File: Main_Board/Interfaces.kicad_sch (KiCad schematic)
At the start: 17 parts, among them J4 External bords interfaces, Q2 2N7002

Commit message: Fix schematic readibility
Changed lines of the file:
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@@
 	(wire
 		(pts
-			(xy 26.67 44.45) (xy 26.67 82.55)
+			(xy 30.48 44.45) (xy 30.48 82.55)
 		)
 		(stroke
@@
 	(wire
 		(pts
-			(xy 123.19 140.97) (xy 127 140.97)
+			(xy 91.44 137.16) (xy 95.25 137.16)
 		)
 		(stroke
@@
 	(wire
 		(pts
-			(xy 123.19 132.08) (xy 127 132.08)
+			(xy 91.44 128.27) (xy 95.25 128.27)
 		)
 		(stroke
@@
 	(wire
 		(pts
-			(xy 77.47 142.24) (xy 85.09 142.24)
+			(xy 45.72 138.43) (xy 53.34 138.43)
 		)
 		(stroke
@@
 	(wire
 		(pts
-			(xy 31.75 44.45) (xy 31.75 80.01)
+			(xy 35.56 44.45) (xy 35.56 80.01)
 		)
 		(stroke
@@
 	(wire
 		(pts
-			(xy 31.75 80.01) (xy 121.92 80.01)
+			(xy 35.56 80.01) (xy 121.92 80.01)
 		)
 		(stroke
@@
 	(wire
 		(pts
-			(xy 77.47 132.08) (xy 85.09 132.08)
+			(xy 45.72 128.27) (xy 53.34 128.27)
 		)
 		(stroke
@@
 	(wire
 		(pts
-			(xy 77.47 137.16) (xy 85.09 137.16)
+			(xy 45.72 133.35) (xy 53.34 133.35)
 		)
 		(stroke
@@
 	(wire
 		(pts
-			(xy 26.67 82.55) (xy 142.24 82.55)
+			(xy 30.48 82.55) (xy 142.24 82.55)
 		)
 		(stroke
@@
 	)
 	(label "B_RS485"
-		(at 127 140.97 0)
+		(at 95.25 137.16 0)
 		(effects
 			(font
@@
 	)
 	(label "A_RS485"
-		(at 127 132.08 0)
+		(at 95.25 128.27 0)
 		(effects
 			(font
@@
 	(hierarchical_label "MODULE_BUS_RX"
 		(shape input)
-		(at 77.47 137.16 180)
+		(at 45.72 133.35 180)
 		(effects
 			(font
@@
 	(hierarchical_label "MODULE_BUS_DIR"
 		(shape input)
-		(at 77.47 142.24 180)
+		(at 45.72 138.43 180)
 		(effects
 			(font
@@
 	(hierarchical_label "MODULE_BUS_TX"
 		(shape output)
-		(at 77.47 132.08 180)
+		(at 45.72 128.27 180)
 		(effects
 			(font
@@
 	(symbol
 		(lib_id "power:+3V3")
-		(at 26.67 44.45 0)
+		(at 30.48 44.45 0)
 		(unit 1)
 		(body_style 1)
@@
 		(dnp no)
 		(property "Reference" "#PWR069"
-			(at 26.67 48.26 0)
+			(at 30.48 48.26 0)
 			(hide yes)
 			(show_name no)
@@
 		)
 		(property "Value" "+3V3"
-			(at 26.416 39.37 0)
+			(at 30.226 39.37 0)
 			(show_name no)
 			(do_not_autoplace no)
@@
 		)
 		(property "Footprint" ""
-			(at 26.67 44.45 0)
+			(at 30.48 44.45 0)
 			(hide yes)
 			(show_name no)
@@
 		)
 		(property "Datasheet" ""
-			(at 26.67 44.45 0)
+			(at 30.48 44.45 0)
 			(hide yes)
 			(show_name no)
@@
 		)
 		(property "Description" "Power symbol creates a global label with name \"+3V3\""
-			(at 26.67 44.45 0)
+			(at 30.48 44.45 0)
 			(hide yes)
 			(show_name no)
@@
 	(symbol
 		(lib_id "power:+5V")
-		(at 31.75 44.45 0)
+		(at 35.56 44.45 0)
 		(unit 1)
 		(body_style 1)
@@
 		(fields_autoplaced yes)
 		(property "Reference" "#PWR070"
-			(at 31.75 48.26 0)
+			(at 35.56 48.26 0)
 			(hide yes)
 			(show_name no)
@@
 		)
 		(property "Value" "+5V"
-			(at 31.75 39.37 0)
+			(at 35.56 39.37 0)
 			(show_name no)
 			(do_not_autoplace no)
@@
 		)
 		(property "Footprint" ""
-			(at 31.75 44.45 0)
+			(at 35.56 44.45 0)
 			(hide yes)
 			(show_name no)
@@
 		)
 		(property "Datasheet" ""
-			(at 31.75 44.45 0)
+			(at 35.56 44.45 0)
 			(hide yes)
 			(show_name no)
@@
 		)
 		(property "Description" "Power symbol creates a global label with name \"+5V\""
-			(at 31.75 44.45 0)
+			(at 35.56 44.45 0)
 			(hide yes)
 			(show_name no)
@@
 	)
 	(sheet
-		(at 85.09 124.46)
+		(at 53.34 120.65)
 		(size 38.1 24.13)
 		(exclude_from_sim no)
@@
 		)
 		(property "Sheetname" "UART_RS485_Transciever"
-			(at 85.09 123.7484 0)
+			(at 53.34 119.9384 0)
 			(show_name no)
 			(do_not_autoplace no)
@@
 		)
 		(property "Sheetfile" "UART_RS485_Transciever.kicad_sch"
-			(at 85.09 149.1746 0)
+			(at 53.34 145.3646 0)
 			(show_name no)
 			(do_not_autoplace no)
@@
 		)
 		(pin "RS485_B" bidirectional
-			(at 123.19 140.97 0)
+			(at 91.44 137.16 0)
 			(effects
 				(font
@@
 		)
 		(pin "RS485_A" bidirectional
-			(at 123.19 132.08 0)
+			(at 91.44 128.27 0)
 			(effects
 				(font
@@
 		)
 		(pin "TRANSCIEVER_UART_DIR" input
-			(at 85.09 142.24 180)
+			(at 53.34 138.43 180)
 			(effects
 				(font
@@
 		)
 		(pin "TRANSCIEVER_UART_RX" output
-			(at 85.09 137.16 180)
+			(at 53.34 133.35 180)
 			(effects
 				(font
@@
 		)
 		(pin "TRANSCIEVER_UART_TX" input
-			(at 85.09 132.08 180)
+			(at 53.34 128.27 180)
 			(effects
 				(font

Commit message: Change connector footprints
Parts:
- D11: footprint LED_SMD:LED_WS2812B_PLCC4_5.0x5.0mm_P3.2mm -> (none)
- J4: footprint Connector_PinHeader_1.27mm:PinHeader_2x05_P1.27mm_Horizontal -> Connector_PinHeader_1.27mm:PinHeader_2x05_P1.27mm_Vertical
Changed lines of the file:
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@@
 			)
 		)
-		(property "Footprint" "LED_SMD:LED_WS2812B_PLCC4_5.0x5.0mm_P3.2mm"
+		(property "Footprint" ""
 			(at 252.73 59.69 0)
 			(hide yes)
@@
 			)
 		)
-		(property "Footprint" "Connector_PinHeader_1.27mm:PinHeader_2x05_P1.27mm_Horizontal"
+		(property "Footprint" "Connector_PinHeader_1.27mm:PinHeader_2x05_P1.27mm_Vertical"
 			(at 163.83 77.47 0)
 			(hide yes)

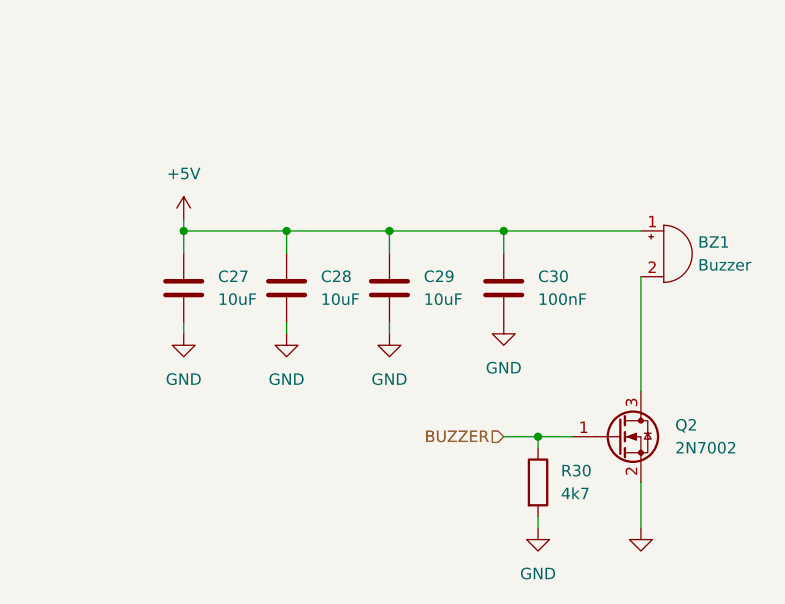
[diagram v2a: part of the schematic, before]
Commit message: Remove buzzer circuitry
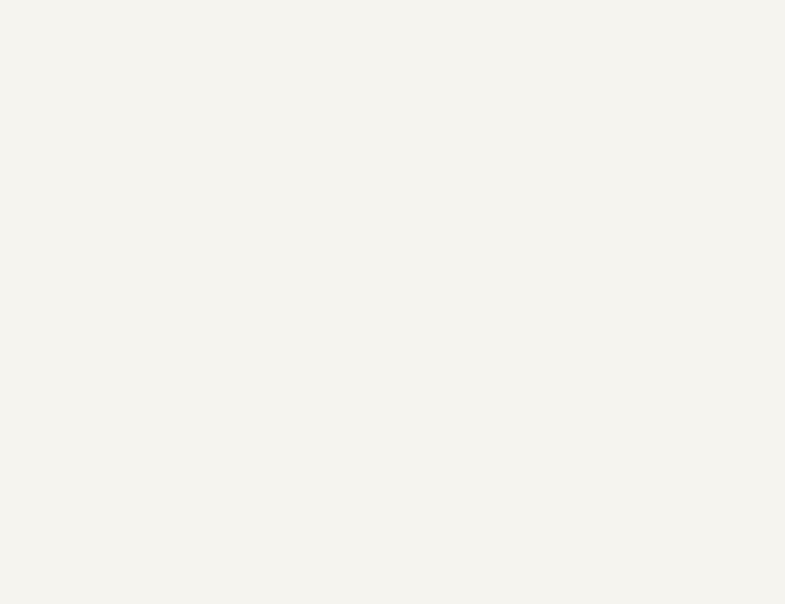
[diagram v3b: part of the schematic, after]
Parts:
- removed BZ1: Buzzer, Buzzer_Beeper:Buzzer_12x9.5RM7.6, symbol Device:Buzzer
- removed C27, C28, C29: 10uF, Capacitor_SMD:C_0603_1608Metric, symbol Device:C
- removed C30: 100nF, Capacitor_SMD:C_0603_1608Metric, symbol Device:C
- removed Q2: 2N7002, Package_TO_SOT_SMD:SOT-23, symbol Transistor_FET:2N7002
- removed R30: 4k7, Resistor_SMD:R_0603_1608Metric, symbol Device:R

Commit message: layout update
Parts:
- removed D10, D9: BAV99, Package_TO_SOT_SMD:SOT-23, symbol Diode:BAV99

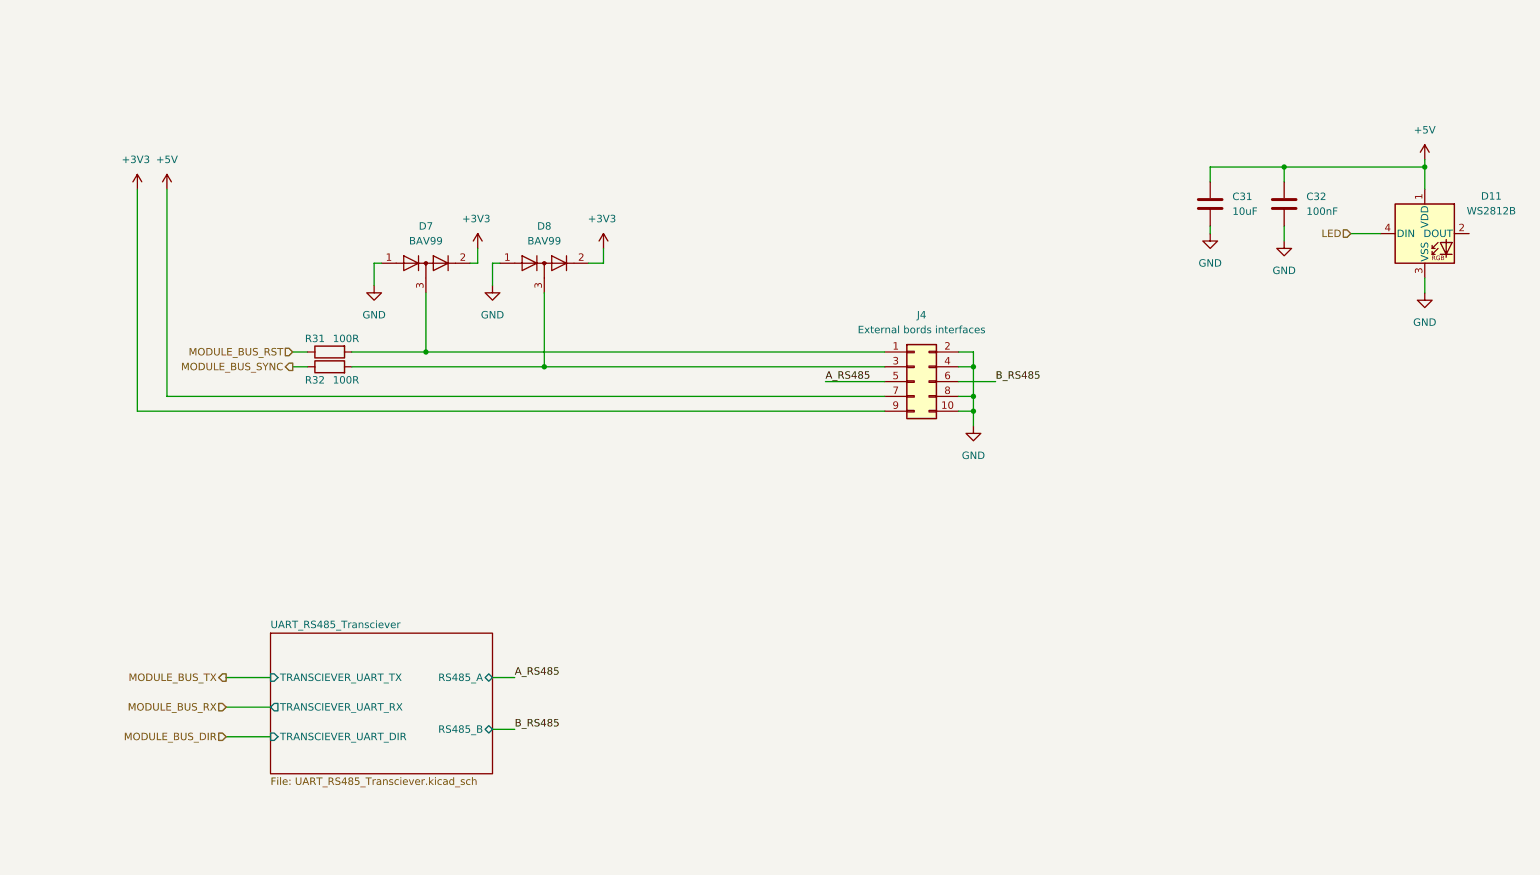
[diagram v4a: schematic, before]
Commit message: Schematic cleanup, ALED footprint + 3D + sch
+ layout and routing
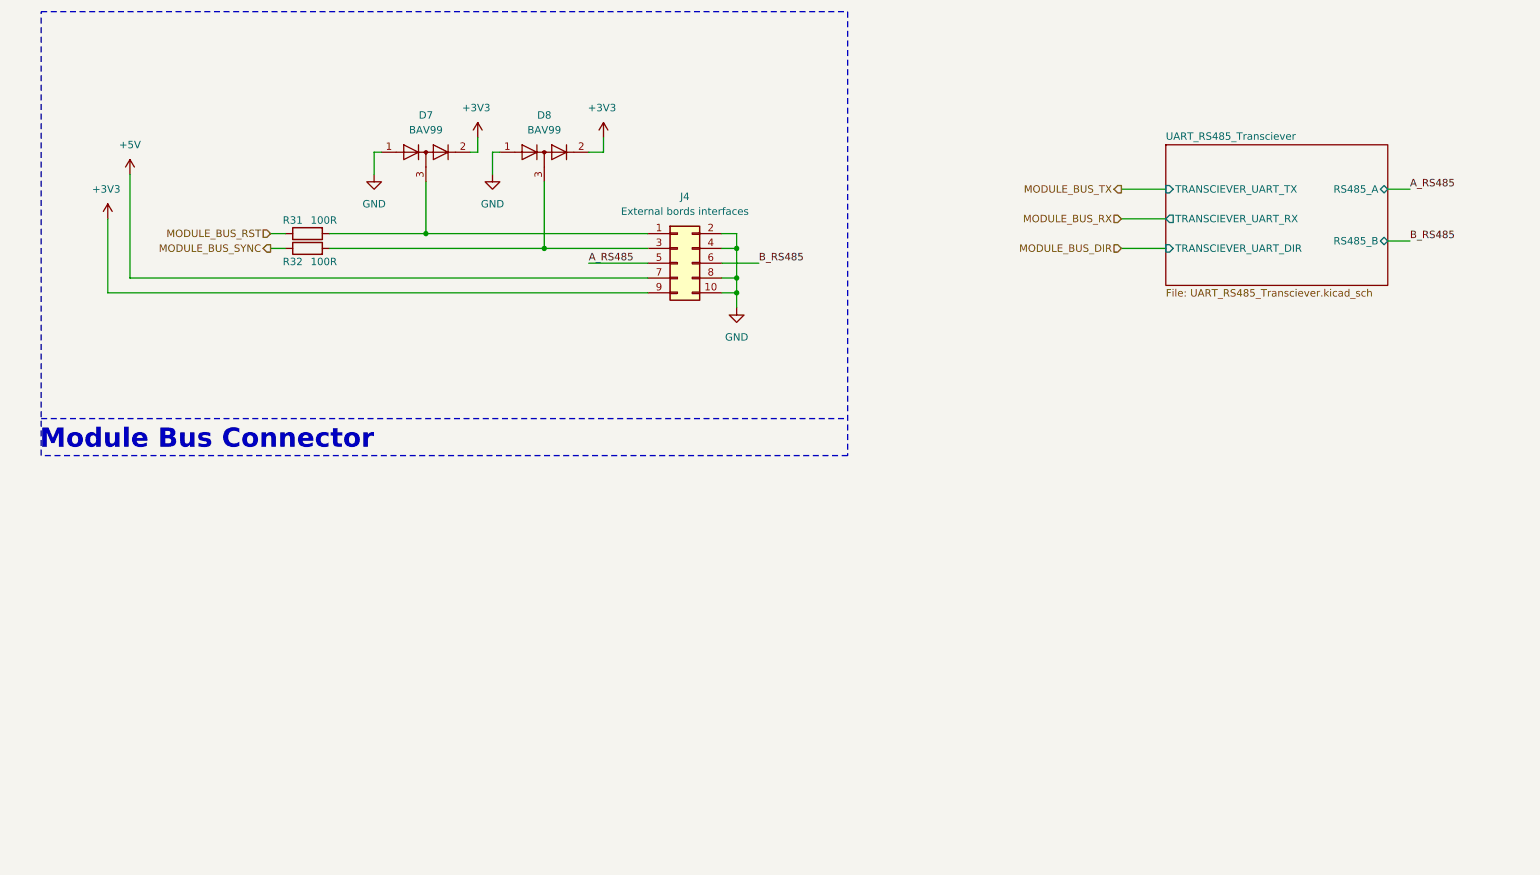
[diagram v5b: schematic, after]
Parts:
- removed C31: 10uF, Capacitor_SMD:C_0603_1608Metric, symbol Device:C
- removed C32: 100nF, Capacitor_SMD:C_0603_1608Metric, symbol Device:C
- removed D11: WS2812B, symbol LED:WS2812B
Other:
- note added: "Module Bus Connector"
- moved on the sheet: D7, D8, J4, R31, R32

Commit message: fix after review -?D7/D8 clamp to 3v3 MB not for 3v3 and other fix
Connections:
- net +3V3: no longer D7.2 (A), D8.2 (A)
- new net +3V3_MB: D7.2 (A), D8.2 (A)
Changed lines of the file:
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@@
+	)
+	(symbol
+		(lib_id "power:+3V3")
+		(at 110.49 35.56 0)
+		(unit 1)
+		(body_style 1)
+		(exclude_from_sim no)
+		(in_bom yes)
+		(on_board yes)
+		(in_pos_files yes)
+		(dnp no)
+		(property "Reference" "#PWR077"
+			(at 110.49 39.37 0)
+			(hide yes)
+			(show_name no)
+			(do_not_autoplace no)
+			(effects
+				(font
+					(size 1.27 1.27)
+				)
+			)
+		)
+		(property "Value" "+3V3_MB"
+			(at 110.49 31.242 0)
+			(show_name no)
+			(do_not_autoplace no)
+			(effects
+				(font
+					(size 1.27 1.27)
+				)
+			)
+		)
+		(property "Footprint" ""
+			(at 110.49 35.56 0)
+			(hide yes)
+			(show_name no)
+			(do_not_autoplace no)
+			(effects
+				(font
+					(size 1.27 1.27)
+				)
+			)
+		)
+		(property "Datasheet" ""
+			(at 110.49 35.56 0)
+			(hide yes)
+			(show_name no)
+			(do_not_autoplace no)
+			(effects
+				(font
+					(size 1.27 1.27)
+				)
+			)
+		)
+		(property "Description" "Power symbol creates a global label with name \"+3V3\""
+			(at 110.49 35.56 0)
+			(hide yes)
+			(show_name no)
+			(do_not_autoplace no)
+			(effects
+				(font
+					(size 1.27 1.27)
+				)
+			)
+		)
+		(pin "1"
+		)
+		(instances
+			(project "Main_Board"
+				(path "/7481738f-7c20-40bb-99b0-6ccd4168db33/f339aa79-d1b1-4b60-b951-815db04e9281"
+					(reference "#PWR077")
+					(unit 1)
+				)
+			)
+		)
+	)
+	(symbol
+		(lib_id "power:+3V3")
+		(at 88.9 35.56 0)
+		(unit 1)
+		(body_style 1)
+		(exclude_from_sim no)
+		(in_bom yes)
+		(on_board yes)
+		(in_pos_files yes)
+		(dnp no)
+		(property "Reference" "#PWR075"
+			(at 88.9 39.37 0)
+			(hide yes)
+			(show_name no)
+			(do_not_autoplace no)
+			(effects
+				(font
+					(size 1.27 1.27)
+				)
+			)
+		)
+		(property "Value" "+3V3_MB"
+			(at 88.9 31.242 0)
+			(show_name no)
+			(do_not_autoplace no)
+			(effects
+				(font
+					(size 1.27 1.27)
+				)
+			)
+		)
+		(property "Footprint" ""
+			(at 88.9 35.56 0)
+			(hide yes)
+			(show_name no)
+			(do_not_autoplace no)
+			(effects
+				(font
+					(size 1.27 1.27)
+				)
+			)
+		)
+		(property "Datasheet" ""
+			(at 88.9 35.56 0)
+			(hide yes)
+			(show_name no)
+			(do_not_autoplace no)
+			(effects
+				(font
+					(size 1.27 1.27)
+				)
+			)
+		)
+		(property "Description" "Power symbol creates a global label with name \"+3V3\""
+			(at 88.9 35.56 0)
+			(hide yes)
+			(show_name no)
+			(do_not_autoplace no)
+			(effects
+				(font
+					(size 1.27 1.27)
+				)
+			)
+		)
+		(pin "1"
+		)
+		(instances
+			(project "Main_Board"
+				(path "/7481738f-7c20-40bb-99b0-6ccd4168db33/f339aa79-d1b1-4b60-b951-815db04e9281"
+					(reference "#PWR075")
+					(unit 1)
+				)
+			)
+		)
 	)
 	(symbol
@@
 	)
 	(symbol
-		(lib_id "power:+3V3")
-		(at 110.49 35.56 0)
-		(unit 1)
-		(body_style 1)
-		(exclude_from_sim no)
-		(in_bom yes)
-		(on_board yes)
-		(in_pos_files yes)
-		(dnp no)
-		(property "Reference" "#PWR077"
-			(at 110.49 39.37 0)
-			(hide yes)
-			(show_name no)
-			(do_not_autoplace no)
-			(effects
-				(font
-					(size 1.27 1.27)
-				)
-			)
-		)
-		(property "Value" "+3V3"
-			(at 110.236 30.48 0)
-			(show_name no)
-			(do_not_autoplace no)
-			(effects
-				(font
-					(size 1.27 1.27)
-				)
-			)
-		)
-		(property "Footprint" ""
-			(at 110.49 35.56 0)
-			(hide yes)
-			(show_name no)
-			(do_not_autoplace no)
-			(effects
-				(font
-					(size 1.27 1.27)
-				)
-			)
-		)
-		(property "Datasheet" ""
-			(at 110.49 35.56 0)
-			(hide yes)
-			(show_name no)
-			(do_not_autoplace no)
-			(effects
-				(font
-					(size 1.27 1.27)
-				)
-			)
-		)
-		(property "Description" "Power symbol creates a global label with name \"+3V3\""
-			(at 110.49 35.56 0)
-			(hide yes)
-			(show_name no)
-			(do_not_autoplace no)
-			(effects
-				(font
-					(size 1.27 1.27)
-				)
-			)
-		)
-		(pin "1"
-		)
-		(instances
-			(project "Main_Board"
-				(path "/7481738f-7c20-40bb-99b0-6ccd4168db33/f339aa79-d1b1-4b60-b951-815db04e9281"
-					(reference "#PWR077")
-					(unit 1)
-				)
-			)
-		)
-	)
-	(symbol
 		(lib_id "Diode:BAV99")
 		(at 100.33 38.1 0)
@@
 					(unit 1)
 				)
-			)
-		)
-	)
-	(symbol
-		(lib_id "power:+3V3")
-		(at 88.9 35.56 0)
-		(unit 1)
-		(body_style 1)
-		(exclude_from_sim no)
-		(in_bom yes)
-		(on_board yes)
-		(in_pos_files yes)
-		(dnp no)
-		(property "Reference" "#PWR075"
-			(at 88.9 39.37 0)
-			(hide yes)
-			(show_name no)
-			(do_not_autoplace no)
-			(effects
-				(font
-					(size 1.27 1.27)
-				)
-			)
-		)
-		(property "Value" "+3V3"
-			(at 88.646 30.48 0)
-			(show_name no)
-			(do_not_autoplace no)
-			(effects
-				(font
-					(size 1.27 1.27)
-				)
-			)
-		)
-		(property "Footprint" ""
-			(at 88.9 35.56 0)
-			(hide yes)
-			(show_name no)
-			(do_not_autoplace no)
-			(effects
-				(font
-					(size 1.27 1.27)
-				)
-			)
-		)
-		(property "Datasheet" ""
-			(at 88.9 35.56 0)
-			(hide yes)
-			(show_name no)
-			(do_not_autoplace no)
-			(effects
-				(font
-					(size 1.27 1.27)
-				)
-			)
-		)
-		(property "Description" "Power symbol creates a global label with name \"+3V3\""
-			(at 88.9 35.56 0)
-			(hide yes)
-			(show_name no)
-			(do_not_autoplace no)
-			(effects
-				(font
-					(size 1.27 1.27)
-				)
-			)
-		)
-		(pin "1"
-		)
-		(instances
-			(project "Main_Board"
-				(path "/7481738f-7c20-40bb-99b0-6ccd4168db33/f339aa79-d1b1-4b60-b951-815db04e9281"
-					(reference "#PWR075")
-					(unit 1)
-				)
